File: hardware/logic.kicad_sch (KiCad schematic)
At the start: 22 parts

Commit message: Fixed Logic
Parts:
- removed U?: 4081, symbol 4xxx:4081
- added U?: 4011, symbol 4xxx:4011
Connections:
- net AS_CLOSE_SDC: now also U?.1
- net AS COMMANDS OK: now reaches IC?.7 (~{PRE})
- net AS COMMANDS OK: now also U?.3
- net WD + SAFE OK: now reaches U?.13, U?.2, U?.4
- net at U?.4 (Qa): now also U?.2
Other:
- note added: "CLR: Clear input − Pull low to set Q output low"
- note added: "PRE: Preset input − Pull low to set Q output high"
- note added: "if this pin is low watchdog didn't assert a keep alive signal"
- note added: "pulls outputs low with clear pin if WD or AS signals are not OK"
- moved on the sheet: IC?, U?A, U?D

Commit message: Alpha 1.0.0 Schematic
First Schematic Version for initial checkup
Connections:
- net FLIP FLOP 1 OK: now reaches IC?.5 (Q), U?.8
- net WATCHDOG uC FAULT LATCH: now reaches IC?.3 (~{RES}), IC?.6 (~{CLR}), IC?.7 (~{PRE})
- net FLIP FLOP 2 OK: now reaches IC?.5 (Q), U?.12, U?.9
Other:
- note added: ""OK" means logic 1 on the output"
- note added: "WD operation: Page 7 of Datasheet"
- note added: "if this line is low watchdog didn't assert a keep alive signal"
- note added: "unused"
- note removed: "if this pin is low watchdog didn't assert a keep alive signal"
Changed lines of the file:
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@@
   (junction (at 48.26 149.86) (diameter 0) (color 0 0 0 0)
   )
-  (junction (at 233.68 116.84) (diameter 0) (color 0 0 0 0)
+  (junction (at 241.3 116.84) (diameter 0) (color 0 0 0 0)
   )
   (junction (at 39.37 80.01) (diameter 0) (color 0 0 0 0)
@@
     (stroke (width 0) (type default) (color 0 0 0 0))
   )
-  (wire (pts (xy 233.68 116.84) (xy 233.68 125.73))
+  (wire (pts (xy 241.3 116.84) (xy 241.3 125.73))
     (stroke (width 0) (type default) (color 0 0 0 0))
   )
@@
     (stroke (width 0) (type default) (color 0 0 0 0))
   )
-  (wire (pts (xy 233.68 82.55) (xy 233.68 116.84))
+  (wire (pts (xy 241.3 82.55) (xy 241.3 116.84))
     (stroke (width 0) (type default) (color 0 0 0 0))
   )
@@
     (stroke (width 0) (type default) (color 0 0 0 0))
   )
-  (wire (pts (xy 224.79 116.84) (xy 233.68 116.84))
+  (wire (pts (xy 224.79 116.84) (xy 241.3 116.84))
     (stroke (width 0) (type default) (color 0 0 0 0))
   )
@@
     (stroke (width 0) (type default) (color 0 0 0 0))
   )
-  (wire (pts (xy 233.68 82.55) (xy 248.92 82.55))
+  (wire (pts (xy 241.3 82.55) (xy 248.92 82.55))
     (stroke (width 0) (type default) (color 0 0 0 0))
   )
@@
     (stroke (width 0) (type default) (color 0 0 0 0))
   )
-  (wire (pts (xy 233.68 125.73) (xy 248.92 125.73))
+  (wire (pts (xy 241.3 125.73) (xy 248.92 125.73))
     (stroke (width 0) (type default) (color 0 0 0 0))
   )
@@
     (effects (font (size 1.27 1.27) italic) (justify left bottom))
   )
+  (text "unused" (at 152.4 81.28 0)
+    (effects (font (size 1.27 1.27) italic) (justify left bottom))
+  )
   (text "V_{TH}=1.235V" (at 55.88 139.7 0)
     (effects (font (size 1.27 1.27)) (justify left bottom))
   )
+  (text "\"OK\" means logic 1 on the output" (at 215.9 165.1 0)
+    (effects (font (size 1.27 1.27) italic) (justify left bottom))
+  )
   (text "Watchdog: every 117,5ms MCU plausibility check" (at 83.82 146.05 0)
     (effects (font (size 1.27 1.27) italic) (justify left bottom))
@@
     (effects (font (size 1.27 1.27) italic) (justify left bottom))
   )
-  (text "if this pin is low\nwatchdog didn't assert a keep alive signal"
-    (at 123.19 124.46 0)
+  (text "WD operation:\nPage 7 of Datasheet" (at 99.06 102.87 0)
+    (effects (font (size 1.27 1.27) italic) (justify left bottom))
+  )
+  (text "if this line is low\nwatchdog didn't assert a keep alive signal"
+    (at 133.35 125.73 0)
     (effects (font (size 1.27 1.27) italic) (justify left bottom))
   )
@@
     (effects (font (size 1.27 1.27)) (justify left bottom))
   )
-  (label "AS COMMANDS OK" (at 162.56 62.23 0)
+  (label "AS COMMANDS OK" (at 158.75 62.23 0)
+    (effects (font (size 1.27 1.27)) (justify left bottom))
+  )
+  (label "WD + SAFETY OK" (at 217.17 153.67 0)
+    (effects (font (size 1.27 1.27)) (justify left bottom))
+  )
+  (label "FLIP FLOP 1 OK" (at 232.41 77.47 0)
+    (effects (font (size 1.27 1.27)) (justify left bottom))
+  )
+  (label "WATCHDOG uC FAULT LATCH" (at 146.05 110.49 0)
     (effects (font (size 1.27 1.27)) (justify left bottom))
   )
@@
     (effects (font (size 1.27 1.27)) (justify left bottom))
   )
+  (label "FLIP FLOP 2 OK" (at 224.79 116.84 0)
+    (effects (font (size 1.27 1.27)) (justify left bottom))
+  )

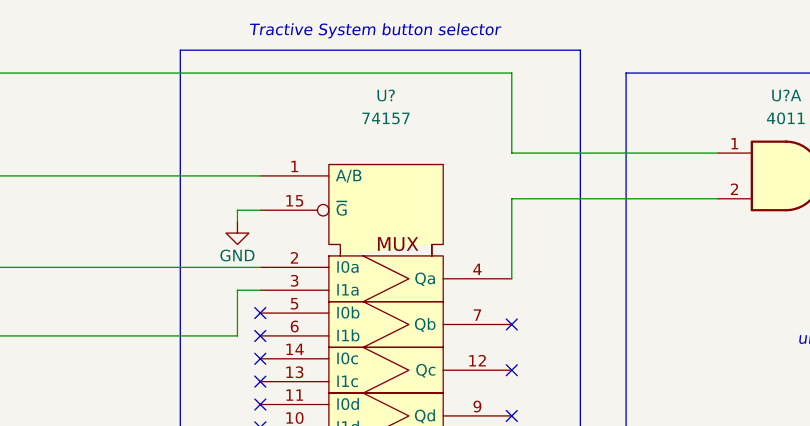
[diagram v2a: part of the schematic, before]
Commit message: Minor changes on v1 schematic
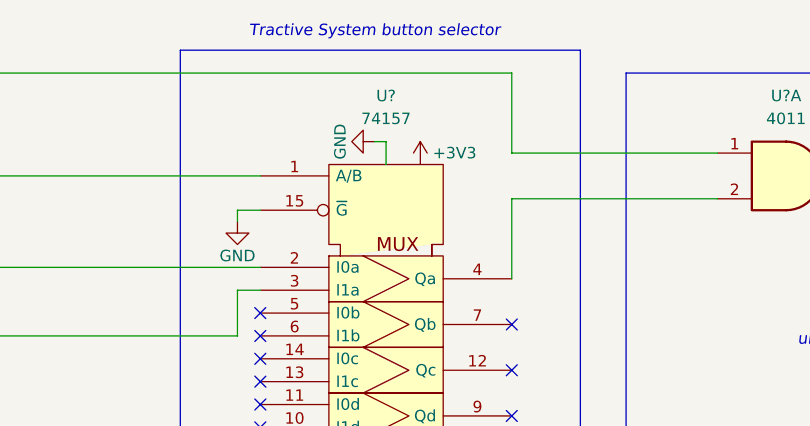
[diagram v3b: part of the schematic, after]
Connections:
- net VCC is gone; now on net +3V3: U?.16 (VCC)
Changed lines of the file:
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@@
+    (stroke (width 0) (type default) (color 0 0 0 0))
+  )
+  (wire (pts (xy 105.41 58.42) (xy 106.68 58.42))
     (stroke (width 0) (type default) (color 0 0 0 0))
   )
@@
   )
   (polyline (pts (xy 54.61 142.24) (xy 54.61 95.25))
+    (stroke (width 0) (type default) (color 0 0 0 0))
+  )
+  (wire (pts (xy 106.68 58.42) (xy 106.68 60.96))
     (stroke (width 0) (type default) (color 0 0 0 0))
   )
@@
     (pin "7")
   )
+  (symbol (lib_id "power:GND") (at 105.41 58.42 270) (unit 1)
+    (in_bom yes) (on_board yes)
+    (property "Reference" "#PWR?" (id 0) (at 99.06 58.42 0)
+      (effects (font (size 1.27 1.27)) hide)
+    )
+    (property "Value" "GND" (id 1) (at 101.6 58.42 0))
+    (property "Footprint" "" (id 2) (at 105.41 58.42 0)
+      (effects (font (size 1.27 1.27)) hide)
+    )
+    (property "Datasheet" "" (id 3) (at 105.41 58.42 0)
+      (effects (font (size 1.27 1.27)) hide)
+    )
+    (pin "1")
+  )
   (symbol (lib_id "SamacSys_Parts:UCC2946DG4") (at 93.98 110.49 0) (unit 1)
     (in_bom yes) (on_board yes)
@@
     (pin "3")
   )
+  (symbol (lib_id "power:+3V3") (at 110.49 60.96 0) (unit 1)
+    (in_bom yes) (on_board yes)
+    (property "Reference" "#PWR?" (id 0) (at 110.49 64.77 0)
+      (effects (font (size 1.27 1.27)) hide)
+    )
+    (property "Value" "+3V3" (id 1) (at 114.3 59.69 0))
+    (property "Footprint" "" (id 2) (at 110.49 60.96 0)
+      (effects (font (size 1.27 1.27)) hide)
+    )
+    (property "Datasheet" "" (id 3) (at 110.49 60.96 0)
+      (effects (font (size 1.27 1.27)) hide)
+    )
+    (pin "1")
+  )
   (symbol (lib_id "Device:C_Small") (at 88.9 130.81 0) (unit 1)

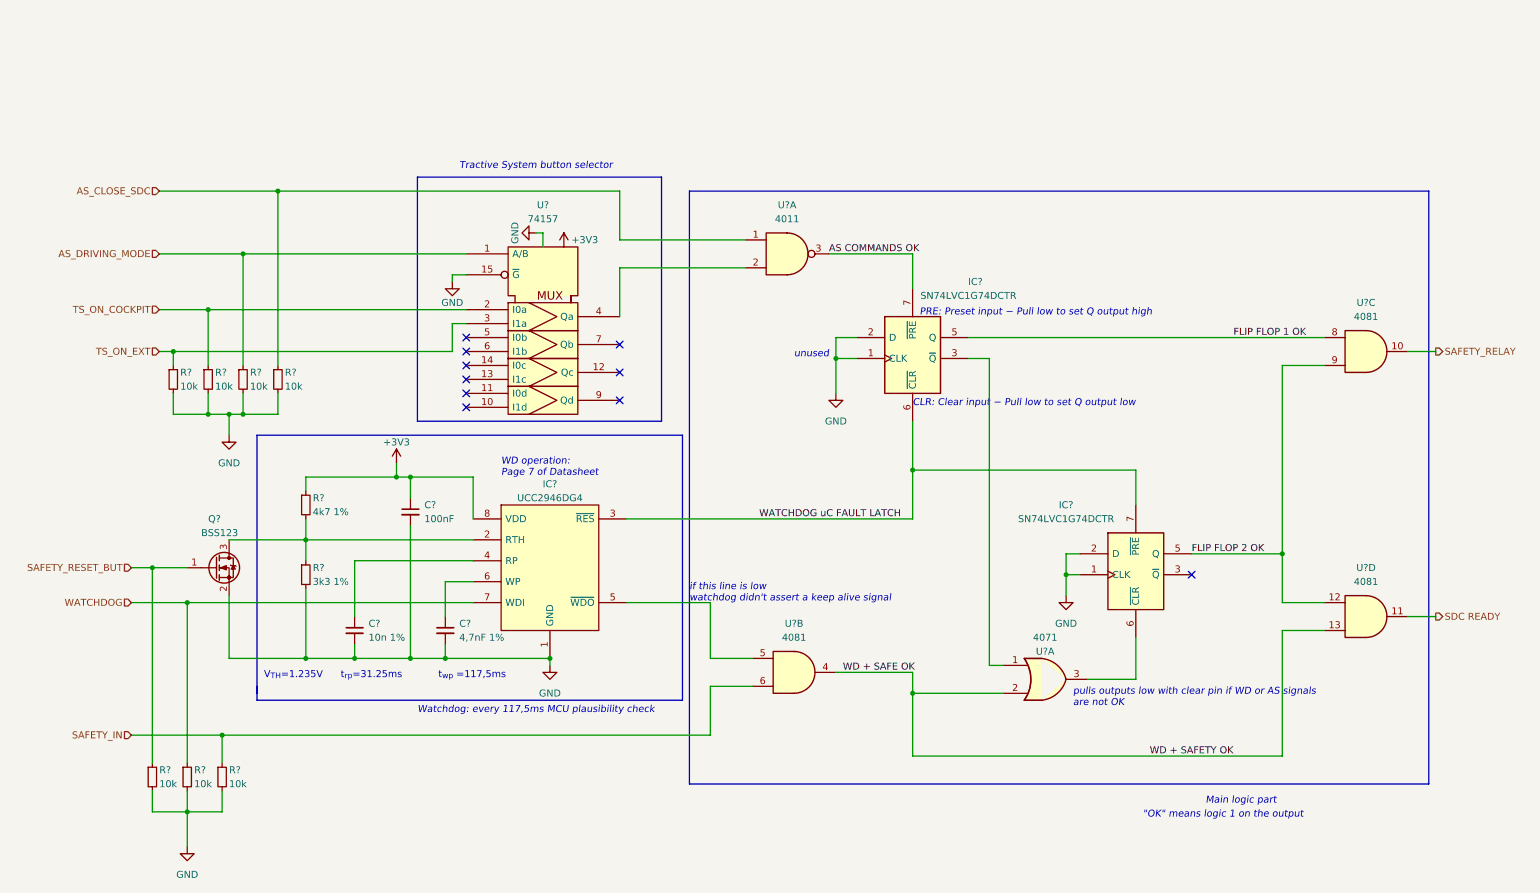
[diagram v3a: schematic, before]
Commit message: minor schematic cleanup
Fixes before second review
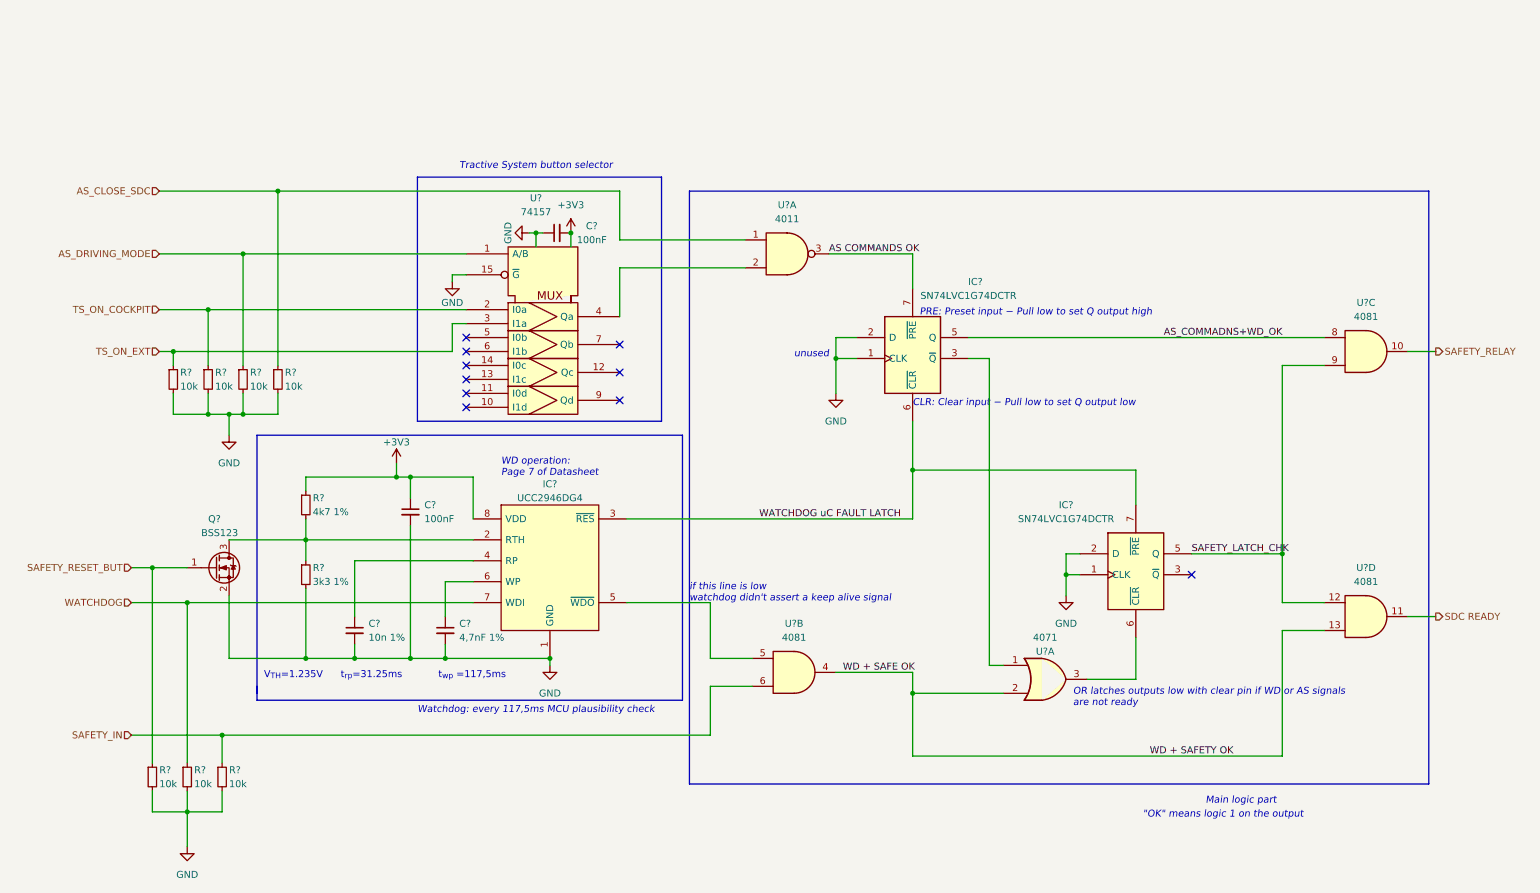
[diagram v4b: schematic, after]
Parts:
- added C?: 100nF, symbol Device:C_Small
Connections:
- net +3V3: now also C?.2
- net GND: now also C?.1
- net FLIP FLOP 1 OK renamed AS_COMMADNS+WD_OK
- net FLIP FLOP 2 OK renamed SAFETY_LATCH_CHK
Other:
- note added: "OR latches outputs low with clear pin if WD or AS signals are not ready"
- note removed: "pulls outputs low with clear pin if WD or AS signals are not OK"
- company: (none) -> PUT Motorsport
- title: (none) -> EBS Hard Wired Logic
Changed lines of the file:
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@@
 (kicad_sch (version 20211123) (generator eeschema)
   (paper "A4")
+  (title_block
+    (title "EBS Hard Wired Logic")
+    (date "2022-10-29")
+    (rev "Beta 1.1")
+    (company "PUT Motorsport")
+  )
+  (junction (at 111.76 58.42) (diameter 0) (color 0 0 0 0)
+  )
   (junction (at 58.42 50.8) (diameter 0) (color 0 0 0 0)
   )
@@
   )
   (junction (at 41.91 163.83) (diameter 0) (color 0 0 0 0)
+  )
+  (junction (at 105.41 58.42) (diameter 0) (color 0 0 0 0)
   )
   (junction (at 173.99 101.6) (diameter 0) (color 0 0 0 0)
@@
     (stroke (width 0) (type default) (color 0 0 0 0))
   )
+  (wire (pts (xy 105.41 58.42) (xy 106.68 58.42))
+    (stroke (width 0) (type default) (color 0 0 0 0))
+  )
   (wire (pts (xy 41.91 125.73) (xy 41.91 154.94))
     (stroke (width 0) (type default) (color 0 0 0 0))
@@
     (stroke (width 0) (type default) (color 0 0 0 0))
   )
-  (wire (pts (xy 105.41 58.42) (xy 106.68 58.42))
+  (wire (pts (xy 104.14 58.42) (xy 105.41 58.42))
     (stroke (width 0) (type default) (color 0 0 0 0))
   )
@@
     (stroke (width 0) (type default) (color 0 0 0 0))
   )
-  (wire (pts (xy 106.68 58.42) (xy 106.68 60.96))
+  (wire (pts (xy 105.41 58.42) (xy 105.41 60.96))
     (stroke (width 0) (type default) (color 0 0 0 0))
   )
@@
     (stroke (width 0) (type default) (color 0 0 0 0))
   )
+  (wire (pts (xy 111.76 58.42) (xy 111.76 60.96))
+    (stroke (width 0) (type default) (color 0 0 0 0))
+  )
   (wire (pts (xy 72.39 128.27) (xy 72.39 118.11))
     (stroke (width 0) (type default) (color 0 0 0 0))
@@
     (stroke (width 0) (type default) (color 0 0 0 0))
   )
-  (text "pulls outputs low with clear pin if WD or AS signals\nare not OK"
+  (text "OR latches outputs low with clear pin if WD or AS signals\nare not ready\n"
     (at 203.2 144.78 0)
     (effects (font (size 1.27 1.27) italic) (justify left bottom))
@@
     (effects (font (size 1.27 1.27)) (justify left bottom))
   )
-  (label "FLIP FLOP 1 OK" (at 232.41 77.47 0)
+  (label "AS_COMMADNS+WD_OK" (at 219.71 77.47 0)
     (effects (font (size 1.27 1.27)) (justify left bottom))
   )
@@
     (effects (font (size 1.27 1.27)) (justify left bottom))
   )
-  (label "FLIP FLOP 2 OK" (at 224.79 116.84 0)
+  (label "SAFETY_LATCH_CHK" (at 224.79 116.84 0)
     (effects (font (size 1.27 1.27)) (justify left bottom))
   )
@@
     (pin "7")
   )
-  (symbol (lib_id "power:GND") (at 105.41 58.42 270) (unit 1)
-    (in_bom yes) (on_board yes)
-    (property "Reference" "#PWR?" (id 0) (at 99.06 58.42 0)
-      (effects (font (size 1.27 1.27)) hide)
-    )
-    (property "Value" "GND" (id 1) (at 101.6 58.42 0))
-    (property "Footprint" "" (id 2) (at 105.41 58.42 0)
-      (effects (font (size 1.27 1.27)) hide)
-    )
-    (property "Datasheet" "" (id 3) (at 105.41 58.42 0)
-      (effects (font (size 1.27 1.27)) hide)
-    )
-    (pin "1")
+  (symbol (lib_id "power:GND") (at 104.14 58.42 270) (unit 1)
+    (in_bom yes) (on_board yes)
+    (property "Reference" "#PWR?" (id 0) (at 97.79 58.42 0)
+      (effects (font (size 1.27 1.27)) hide)
+    )
+    (property "Value" "GND" (id 1) (at 100.33 58.42 0))
+    (property "Footprint" "" (id 2) (at 104.14 58.42 0)
+      (effects (font (size 1.27 1.27)) hide)
+    )
+    (property "Datasheet" "" (id 3) (at 104.14 58.42 0)
+      (effects (font (size 1.27 1.27)) hide)
+    )
+    (pin "1")
+  )
+  (symbol (lib_id "Device:C_Small") (at 109.22 58.42 90) (unit 1)
+    (in_bom yes) (on_board yes)
+    (property "Reference" "C?" (id 0) (at 115.57 57.15 90))
+    (property "Value" "100nF" (id 1) (at 115.57 59.69 90))
+    (property "Footprint" "" (id 2) (at 109.22 58.42 0)
+      (effects (font (size 1.27 1.27)) hide)
+    )
+    (property "Datasheet" "~" (id 3) (at 109.22 58.42 0)
+      (effects (font (size 1.27 1.27)) hide)
+    )
+    (pin "1")
+    (pin "2")
   )
   (symbol (lib_id "SamacSys_Parts:UCC2946DG4") (at 93.98 110.49 0) (unit 1)
@@
   (symbol (lib_id "74xx_IEEE:74157") (at 106.68 76.2 0) (unit 1)
     (in_bom yes) (on_board yes)
-    (property "Reference" "U?" (id 0) (at 106.68 53.34 0))
-    (property "Value" "74157" (id 1) (at 106.68 55.88 0))
+    (property "Reference" "U?" (id 0) (at 105.41 52.07 0))
+    (property "Value" "74157" (id 1) (at 105.41 54.61 0))
     (property "Footprint" "" (id 2) (at 106.68 76.2 0)
       (effects (font (size 1.27 1.27)) hide)
@@
     (pin "3")
   )
-  (symbol (lib_id "power:+3V3") (at 110.49 60.96 0) (unit 1)
-    (in_bom yes) (on_board yes)
-    (property "Reference" "#PWR?" (id 0) (at 110.49 64.77 0)
-      (effects (font (size 1.27 1.27)) hide)
-    )
-    (property "Value" "+3V3" (id 1) (at 114.3 59.69 0))
-    (property "Footprint" "" (id 2) (at 110.49 60.96 0)
-      (effects (font (size 1.27 1.27)) hide)
-    )
-    (property "Datasheet" "" (id 3) (at 110.49 60.96 0)
-      (effects (font (size 1.27 1.27)) hide)
-    )
+  (symbol (lib_id "power:+3V3") (at 111.76 58.42 0) (unit 1)
+    (in_bom yes) (on_board yes)
+    (property "Reference" "#PWR?" (id 0) (at 111.76 62.23 0)
+      (effects (font (size 1.27 1.27)) hide)
+    )
+    (property "Value" "+3V3" (id 1) (at 111.76 53.34 0))
+    (property "Footprint" "" (id 2) (at 111.76 58.42 0)
+      (effects (font (size 1.27 1.27)) hide)
+    )
+    (property "Datasheet" "" (id 3) (at 111.76 58.42 0)
+      (effects (font (size 1.27 1.27)) hide)
+    )

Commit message: Schematic ready for second review
Cleaned up, numerated, added footprints, JW notes considered
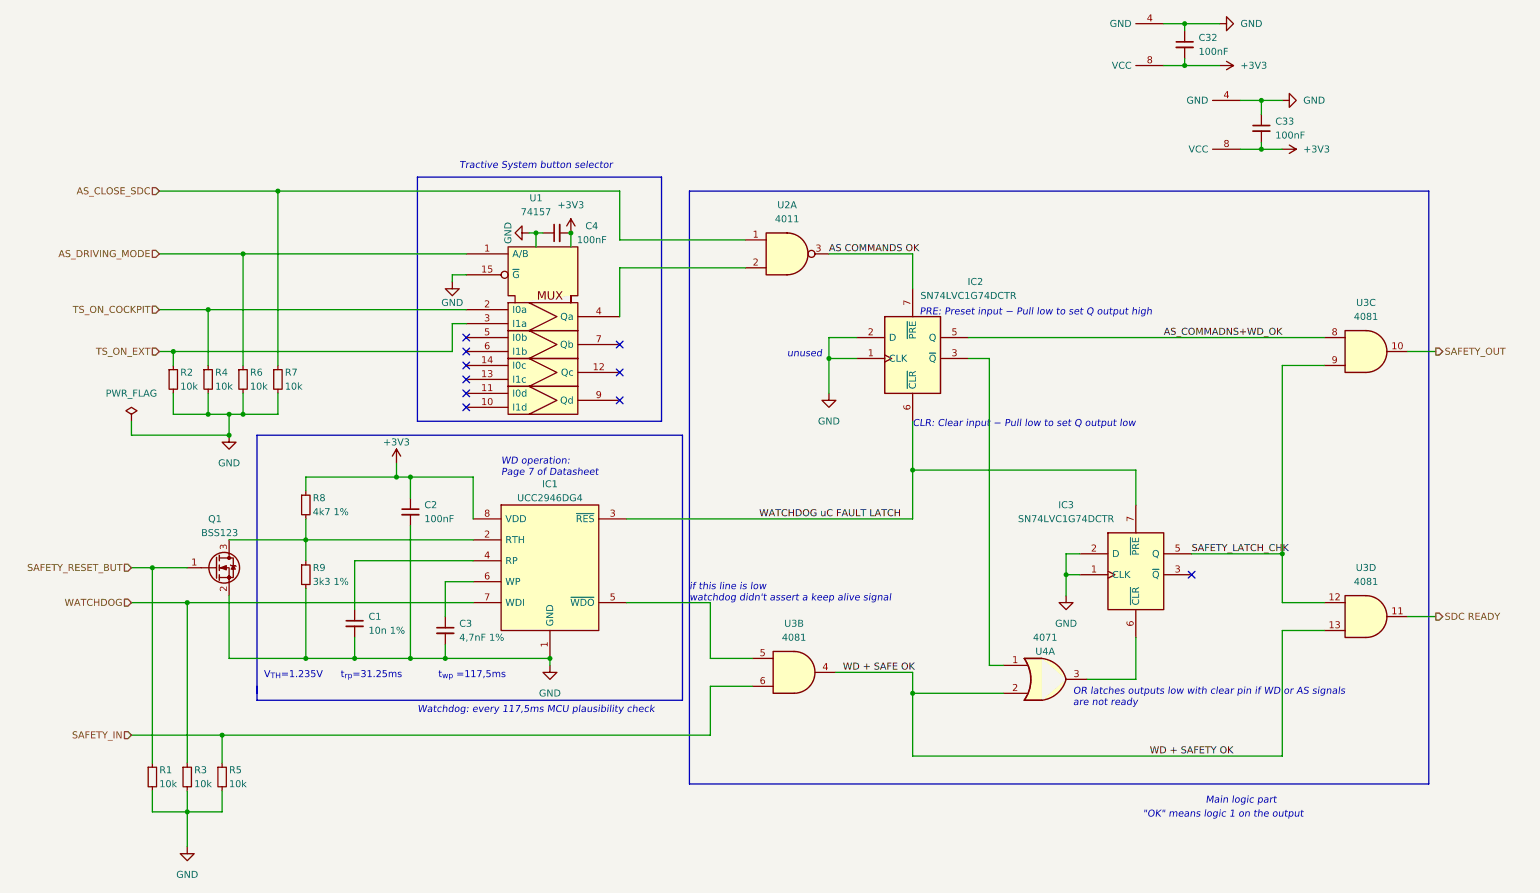
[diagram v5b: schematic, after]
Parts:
- added C32, C33: 100nF, Capacitor_SMD:C_0201_0603Metric_Pad0.64x0.40mm_HandSolder, symbol Device:C_Small
- C1, C2, C3, C4: renamed from C?; footprint (none) -> Capacitor_SMD:C_0201_0603Metric_Pad0.64x0.40mm_HandSolder
- IC1: renamed from IC?; footprint SOIC127P600X175-8N -> SamacSys_Parts:SOIC127P600X175-8N
- IC2, IC3: renamed from IC?; footprint SOP65P400X130-8N -> SamacSys_Parts:SOP65P400X130-8N
- R1, R2, R3, R4, R5, R6, R7, R8, R9: renamed from R?; footprint (none) -> Resistor_SMD:R_0603_1608Metric
- U1: renamed from U?; footprint (none) -> Resistor_SMD:R_0603_1608Metric
- gave numbers to parts that had none: 4
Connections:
- net +3V3: now also IC2.8 (VCC), IC3.8 (VCC), C32.2, C33.2
- net GND: now also IC2.4 (GND), IC3.4 (GND), C32.1, C33.1
- net SAFETY_RELAY renamed SAFETY_OUT
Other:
- moved on the sheet: C1
